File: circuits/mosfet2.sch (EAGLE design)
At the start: 24 parts, among them IC2 IR4427S, J1 Power In 12V, J2 BED 24V, J3 Head 12V, J4 PSU GND, Q1 AOT240L, Q2 AOT240L

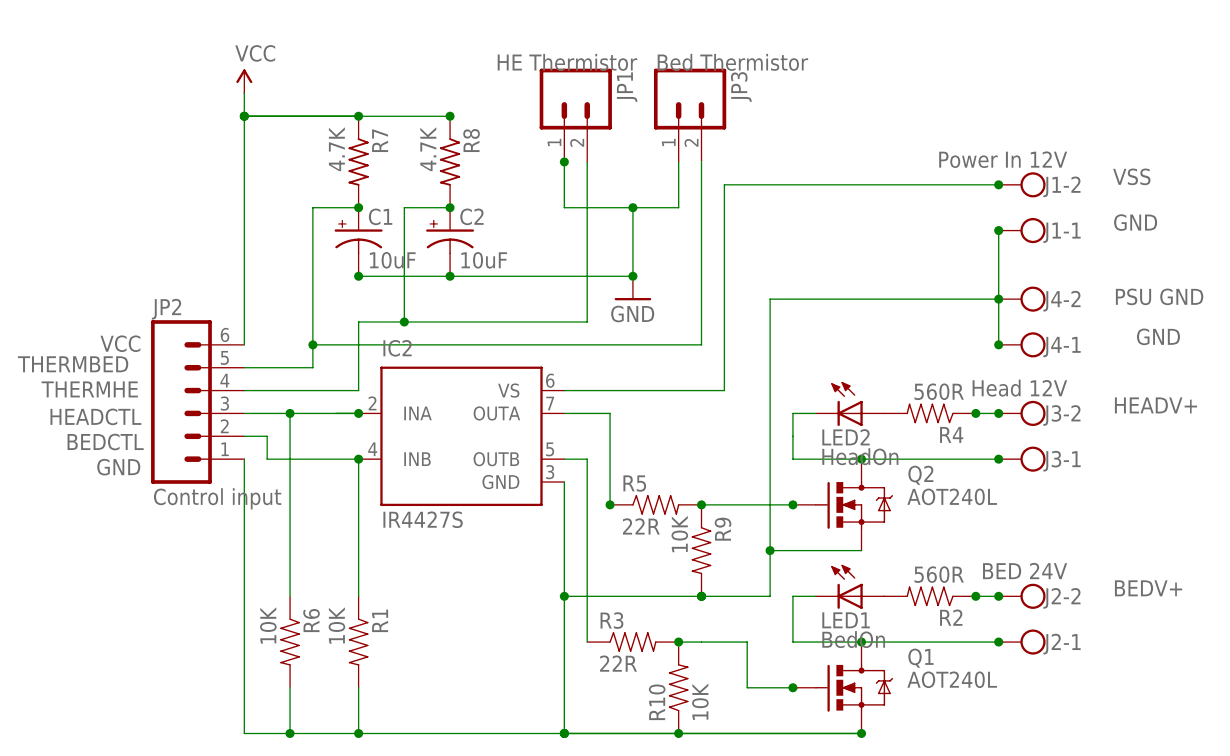
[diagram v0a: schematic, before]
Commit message: update mosfet circuit
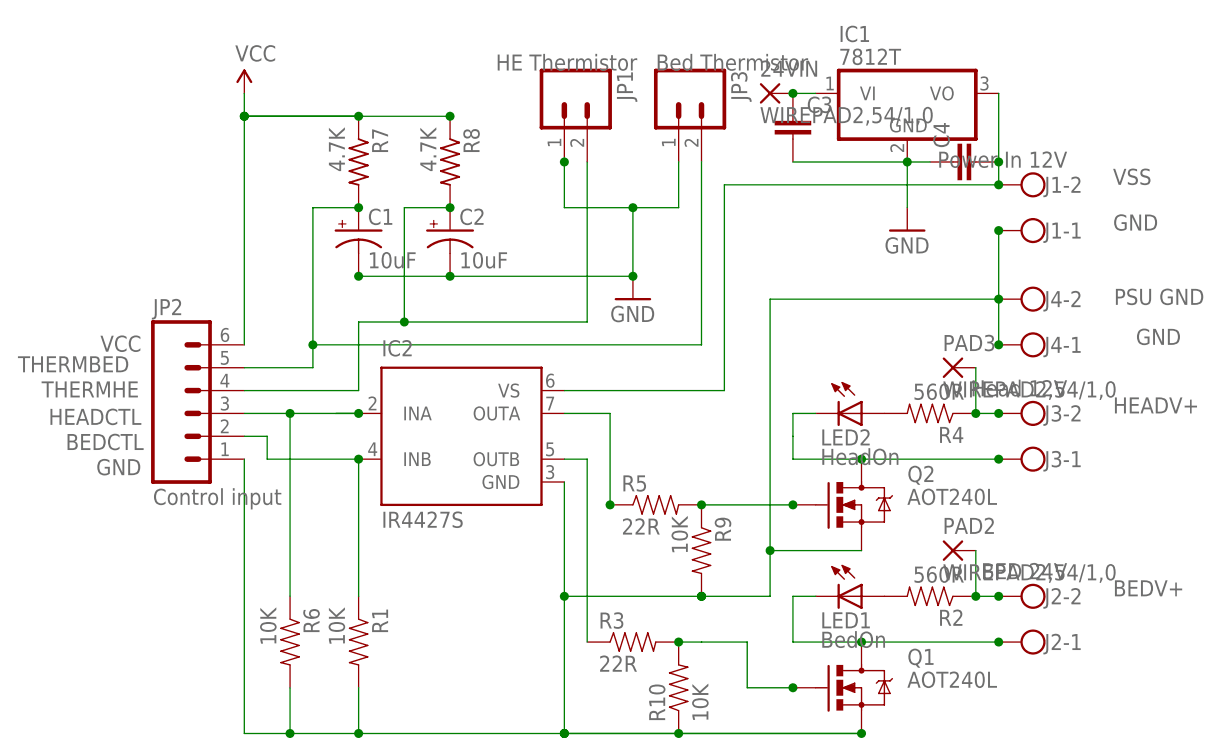
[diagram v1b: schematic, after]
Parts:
- added 24VIN, PAD2, PAD3: WIREPAD2,54/1,0, wirepad:WIREPAD2,54/1,0
- added C3, C4: (no value), SparkFun-Passives:CAPEZ
- added IC1: 7812T, adafruit:7812T
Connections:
- new net N$1: 24VIN.P, C3.1, IC1.VI
- net BEDV+: now also PAD2.P
- net GND: now also C3.2, C4.1, IC1.GND
- net HEADV+: now also PAD3.P
- net VSS: now also C4.2, IC1.VO
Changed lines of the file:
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@@
 <layer number="106" name="bPlate" color="7" fill="1" visible="no" active="yes"/>
 <layer number="107" name="Crop" color="7" fill="1" visible="no" active="yes"/>
+<layer number="108" name="fp8" color="7" fill="1" visible="no" active="yes"/>
+<layer number="109" name="fp9" color="7" fill="1" visible="no" active="yes"/>
+<layer number="110" name="fp0" color="7" fill="1" visible="no" active="yes"/>
+<layer number="111" name="LPC17xx" color="7" fill="1" visible="yes" active="yes"/>
+<layer number="112" name="tSilk" color="7" fill="1" visible="yes" active="yes"/>
 <layer number="116" name="Patch_BOT" color="9" fill="4" visible="no" active="yes"/>
 <layer number="121" name="_tsilk" color="7" fill="1" visible="no" active="yes"/>
 <layer number="122" name="_bsilk" color="7" fill="1" visible="no" active="yes"/>
+<layer number="123" name="tTestmark" color="7" fill="1" visible="no" active="yes"/>
+<layer number="124" name="bTestmark" color="7" fill="1" visible="no" active="yes"/>
 <layer number="125" name="_tNames" color="7" fill="1" visible="no" active="yes"/>
+<layer number="126" name="_bNames" color="7" fill="1" visible="yes" active="yes"/>
+<layer number="127" name="_tValues" color="7" fill="1" visible="yes" active="yes"/>
+<layer number="128" name="_bValues" color="7" fill="1" visible="yes" active="yes"/>
+<layer number="131" name="tAdjust" color="7" fill="1" visible="no" active="yes"/>
+<layer number="132" name="bAdjust" color="7" fill="1" visible="no" active="yes"/>
 <layer number="144" name="Drill_legend" color="7" fill="1" visible="no" active="yes"/>
 <layer number="151" name="HeatSink" color="7" fill="1" visible="no" active="yes"/>
+<layer number="152" name="_bDocu" color="7" fill="1" visible="yes" active="yes"/>
 <layer number="199" name="Contour" color="7" fill="1" visible="no" active="yes"/>
 <layer number="200" name="200bmp" color="1" fill="10" visible="no" active="yes"/>
@@
 <layer number="223" name="223bmp" color="24" fill="1" visible="no" active="no"/>
 <layer number="224" name="224bmp" color="25" fill="1" visible="no" active="no"/>
+<layer number="248" name="Housing" color="7" fill="1" visible="yes" active="yes"/>
+<layer number="249" name="Edge" color="7" fill="1" visible="yes" active="yes"/>
 <layer number="250" name="Descript" color="3" fill="1" visible="no" active="no"/>
 <layer number="251" name="SMDround" color="12" fill="11" visible="no" active="no"/>
@@
 <part name="R9" library="SparkFun-Resistors" deviceset="RESISTOR" device="PTH-1/4W" value="10K"/>
 <part name="R10" library="SparkFun-Resistors" deviceset="RESISTOR" device="PTH-1/4W" value="10K"/>
+<part name="IC1" library="adafruit" deviceset="78*" device="T" technology="12"/>
+<part name="GND2" library="SparkFun-Aesthetics" deviceset="GND" device=""/>
+<part name="24VIN" library="wirepad" deviceset="WIREPAD" device="2,54/1,0"/>
+<part name="PAD2" library="wirepad" deviceset="WIREPAD" device="2,54/1,0"/>
+<part name="PAD3" library="wirepad" deviceset="WIREPAD" device="2,54/1,0"/>
+<part name="C3" library="SparkFun-Passives" deviceset="CAP" device="EZ"/>
+<part name="C4" library="SparkFun-Passives" deviceset="CAP" device="EZ"/>
 </parts>
 <sheets>
@@
 <instance part="R9" gate="G$1" x="2.54" y="48.26" rot="R270"/>
 <instance part="R10" gate="G$1" x="0" y="33.02" rot="R90"/>
+<instance part="IC1" gate="A1" x="25.4" y="99.06"/>
+<instance part="GND2" gate="1" x="25.4" y="83.82"/>
+<instance part="24VIN" gate="G$1" x="10.16" y="99.06"/>
+<instance part="PAD2" gate="G$1" x="30.48" y="48.26"/>
+<instance part="PAD3" gate="G$1" x="30.48" y="68.58"/>
+<instance part="C3" gate="G$1" x="12.7" y="93.98"/>
+<instance part="C4" gate="G$1" x="33.02" y="91.44" rot="R90"/>
 </instances>
 <busses>
@@
 <junction x="-35.56" y="78.74"/>
 </segment>
+<segment>
+<pinref part="IC1" gate="A1" pin="GND"/>
+<pinref part="GND2" gate="1" pin="GND"/>
+<wire x1="25.4" y1="91.44" x2="25.4" y2="86.36" width="0.1524" layer="91"/>
+<pinref part="C3" gate="G$1" pin="2"/>
+<wire x1="12.7" y1="91.44" x2="25.4" y2="91.44" width="0.1524" layer="91"/>
+<junction x="25.4" y="91.44"/>
+<pinref part="C4" gate="G$1" pin="1"/>
+<wire x1="27.94" y1="91.44" x2="25.4" y2="91.44" width="0.1524" layer="91"/>
+</segment>
 </net>
 <net name="N$2" class="0">
@@
 <junction x="35.56" y="43.18"/>
 <junction x="33.02" y="43.18"/>
+<pinref part="PAD2" gate="G$1" pin="P"/>
+<wire x1="33.02" y1="48.26" x2="33.02" y2="43.18" width="0.1524" layer="91"/>
 </segment>
 </net>
@@
 <label x="48.26" y="88.9" size="1.778" layer="95"/>
 <junction x="35.56" y="88.9"/>
+<pinref part="IC1" gate="A1" pin="VO"/>
+<wire x1="35.56" y1="99.06" x2="35.56" y2="91.44" width="0.1524" layer="91"/>
+<pinref part="C4" gate="G$1" pin="2"/>
+<wire x1="35.56" y1="91.44" x2="35.56" y2="88.9" width="0.1524" layer="91"/>
+<junction x="35.56" y="91.44"/>
 </segment>
 </net>
@@
 <junction x="35.56" y="63.5"/>
 <junction x="33.02" y="63.5"/>
+<pinref part="PAD3" gate="G$1" pin="P"/>
+<wire x1="33.02" y1="68.58" x2="33.02" y2="63.5" width="0.1524" layer="91"/>
 </segment>
 </net>
@@
 </segment>
 </net>
+<net name="N$1" class="0">
+<segment>
+<pinref part="IC1" gate="A1" pin="VI"/>
+<pinref part="24VIN" gate="G$1" pin="P"/>
+<wire x1="15.24" y1="99.06" x2="12.7" y2="99.06" width="0.1524" layer="91"/>
+<pinref part="C3" gate="G$1" pin="1"/>
+<junction x="12.7" y="99.06"/>
+</segment>
+</net>
